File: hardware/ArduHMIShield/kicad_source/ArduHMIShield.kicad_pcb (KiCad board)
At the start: 2 copper layers, 72 x 53 mm, 49 parts, among them CN1 ARDUINO, Q1 2N7002, SW1 TAST_VER, SW2 TAST_VER, SW3 TAST_VER, SW4 TAST_VER, SW5 TAST_VER, SW6 TAST_VER, U1 LT1117, U2 74VHC245D

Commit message: updated design files to better support Aisler
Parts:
- C1, C10, C11, C2, C3, C4, C5, C6, C7, C8, C9: value 1u -> 1uF
- C12: value 100n -> 100nF
- R16: value DNI -> 0R
- R19: value 0R -> DNI
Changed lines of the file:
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@@
       (effects (font (size 1 1) (thickness 0.15)))
     )
-    (fp_text value 1u (at 0 1.9 270) (layer F.Fab)
+    (fp_text value 1uF (at 0 1.9 270) (layer F.Fab)
       (effects (font (size 1 1) (thickness 0.15)))
     )
@@
       (effects (font (size 1 1) (thickness 0.15)))
     )
-    (fp_text value 1u (at 0 1.9 270) (layer F.Fab)
+    (fp_text value 1uF (at 0 1.9 270) (layer F.Fab)
       (effects (font (size 1 1) (thickness 0.15)))
     )
@@
       (effects (font (size 1 1) (thickness 0.15)))
     )
-    (fp_text value 1u (at 0 1.9 270) (layer F.Fab)
+    (fp_text value 1uF (at 0 1.9 270) (layer F.Fab)
       (effects (font (size 1 1) (thickness 0.15)))
     )
@@
       (effects (font (size 1 1) (thickness 0.15)))
     )
-    (fp_text value 1u (at 0 1.9 270) (layer F.Fab)
+    (fp_text value 1uF (at 0 1.9 270) (layer F.Fab)
       (effects (font (size 1 1) (thickness 0.15)))
     )
@@
       (effects (font (size 1 1) (thickness 0.15)))
     )
-    (fp_text value 1u (at 0 1.9 180) (layer F.Fab)
+    (fp_text value 1uF (at 0 1.9 180) (layer F.Fab)
       (effects (font (size 1 1) (thickness 0.15)))
     )
@@
       (effects (font (size 1 1) (thickness 0.15)))
     )
-    (fp_text value 1u (at 0 1.9 270) (layer F.Fab)
+    (fp_text value 1uF (at 0 1.9 270) (layer F.Fab)
       (effects (font (size 1 1) (thickness 0.15)))
     )
@@
       (effects (font (size 1 1) (thickness 0.15)))
     )
-    (fp_text value 1u (at 0 1.9) (layer F.Fab)
+    (fp_text value 1uF (at 0 1.9) (layer F.Fab)
       (effects (font (size 1 1) (thickness 0.15)))
     )
@@
       (effects (font (size 1 1) (thickness 0.15)))
     )
-    (fp_text value 1u (at 0 1.9) (layer F.Fab)
+    (fp_text value 1uF (at 0 1.9) (layer F.Fab)
       (effects (font (size 1 1) (thickness 0.15)))
     )
@@
       (effects (font (size 1 1) (thickness 0.15)))
     )
-    (fp_text value 1u (at 0 1.9) (layer F.Fab)
+    (fp_text value 1uF (at 0 1.9) (layer F.Fab)
       (effects (font (size 1 1) (thickness 0.15)))
     )
@@
       (effects (font (size 1 1) (thickness 0.15)))
     )
-    (fp_text value 1u (at 0 1.9 180) (layer F.Fab)
+    (fp_text value 1uF (at 0 1.9 180) (layer F.Fab)
       (effects (font (size 1 1) (thickness 0.15)))
     )
@@
       (effects (font (size 1 1) (thickness 0.15)))
     )
-    (fp_text value 1u (at 0 1.9 180) (layer F.Fab)
+    (fp_text value 1uF (at 0 1.9 180) (layer F.Fab)
       (effects (font (size 1 1) (thickness 0.15)))
     )
@@
       (effects (font (size 1 1) (thickness 0.15)))
     )
-    (fp_text value 100n (at 0 1.9 90) (layer F.Fab)
+    (fp_text value 100nF (at 0 1.9 90) (layer F.Fab)
       (effects (font (size 1 1) (thickness 0.15)))
     )
@@
       (effects (font (size 1 1) (thickness 0.15)))
     )
-    (fp_text value DNI (at 0 1.9 180) (layer F.Fab)
+    (fp_text value 0R (at 0 1.9 180) (layer F.Fab)
       (effects (font (size 1 1) (thickness 0.15)))
     )
@@
       (effects (font (size 1 1) (thickness 0.15)))
     )
-    (fp_text value 0R (at 0 1.9 180) (layer F.Fab)
-      (effects (font (size 1 1) (thickness 0.15)))
-    )
+    (fp_text value DNI (at 0 1.9 180) (layer F.Fab)
+      (effects (font (size 1 1) (thickness 0.15)))
+    )

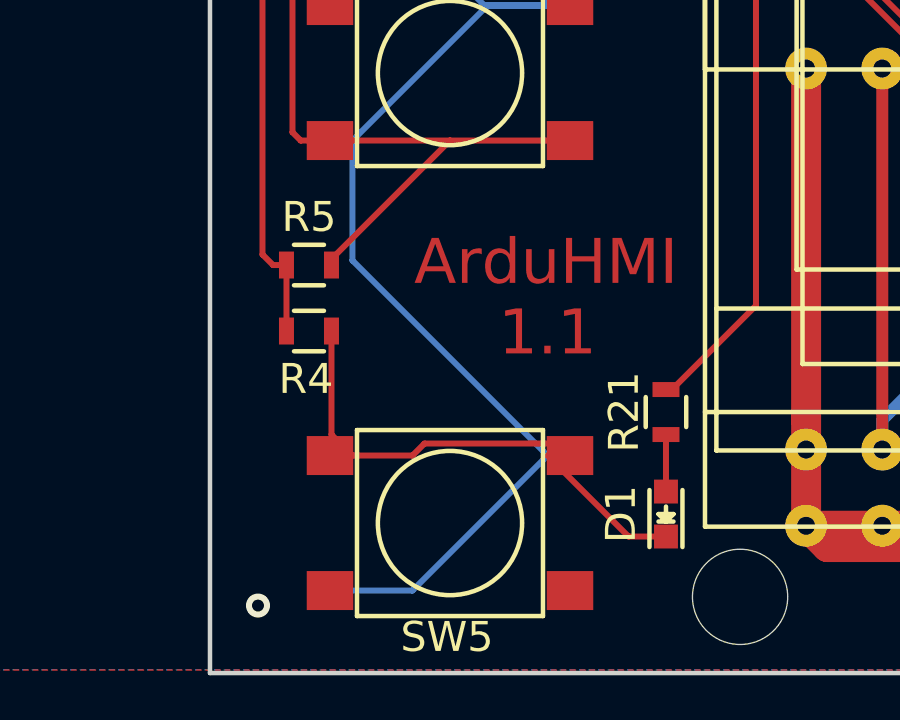
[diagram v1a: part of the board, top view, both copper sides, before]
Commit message: removed short cut, corrected silkscreen
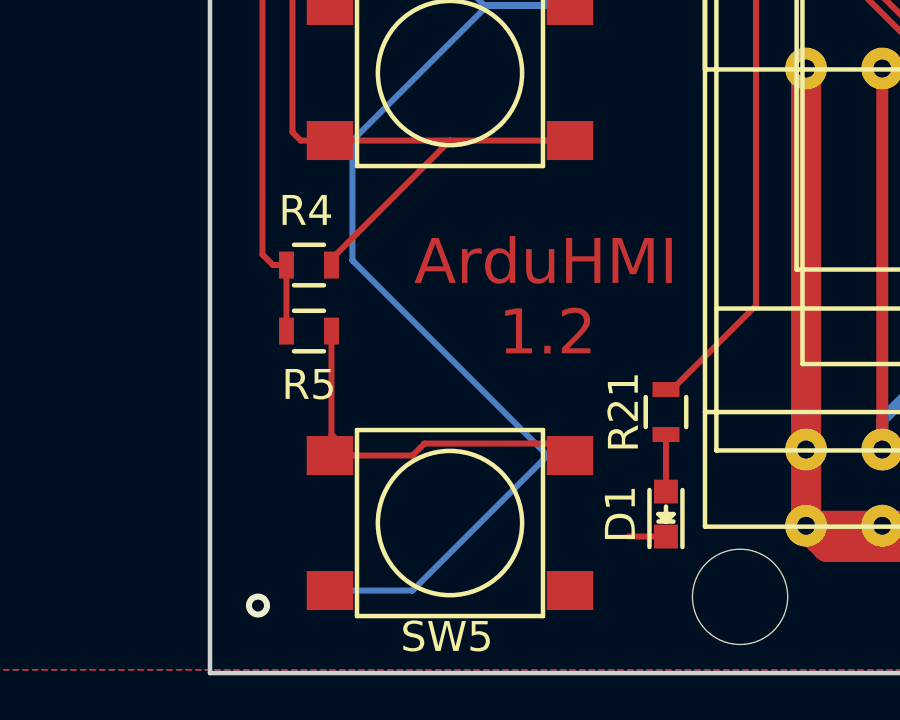
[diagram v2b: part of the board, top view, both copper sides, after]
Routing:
- net GND: track 248.6 -> 244.7 mm
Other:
- board text added: "1.2"
- board text removed: "1.1"
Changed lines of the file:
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@@
     (thickness 1.6)
     (drawings 17)
-    (tracks 516)
+    (tracks 515)
     (zones 0)
     (modules 49)
@@
     (tags "resistor 0603")
     (attr smd)
-    (fp_text reference R4 (at 0.1 -3.8 180) (layer F.SilkS)
+    (fp_text reference R4 (at 0.1 1.8 180) (layer F.SilkS)
       (effects (font (size 1 1) (thickness 0.15)))
     )
@@
     (tags "resistor 0603")
     (attr smd)
-    (fp_text reference R5 (at 0 -3.8) (layer F.SilkS)
+    (fp_text reference R5 (at 0 1.8) (layer F.SilkS)
       (effects (font (size 1 1) (thickness 0.15)))
     )
@@
     (effects (font (size 1.5 1.5) (thickness 0.3)) (justify left))
   )
-  (gr_text 1.1 (at 62.25 118.65) (layer F.Cu)
+  (gr_text 1.2 (at 62.25 118.65) (layer F.Cu)
     (effects (font (size 1.5 1.5) (thickness 0.3)))
   )
@@
   (segment (start 99.1 94.6) (end 104.1 89.6) (width 1) (layer B.Cu) (net 1))
   (segment (start 99.1 100.3) (end 99.1 94.6) (width 1) (layer B.Cu) (net 1))
-  (segment (start 64.95094 125.4493) (end 62.2512 122.74956) (width 0.2) (layer F.Cu) (net 1))
   (segment (start 66.2 125.4493) (end 64.95094 125.4493) (width 0.2) (layer F.Cu) (net 1))
   (via (at 52.5 80) (size 0.8) (drill 0.4) (layers F.Cu B.Cu) (net 1))

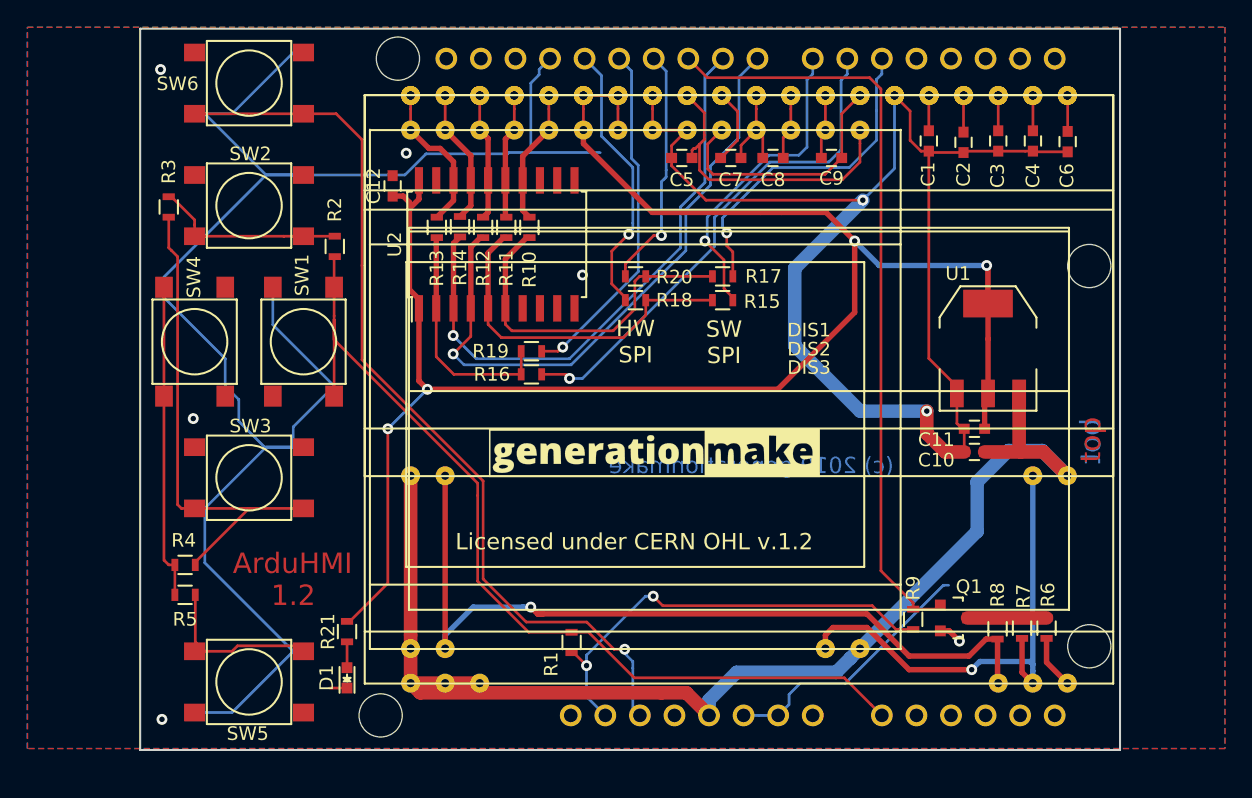
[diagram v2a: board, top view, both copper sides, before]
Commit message: added Arduino SPI header, updated all files
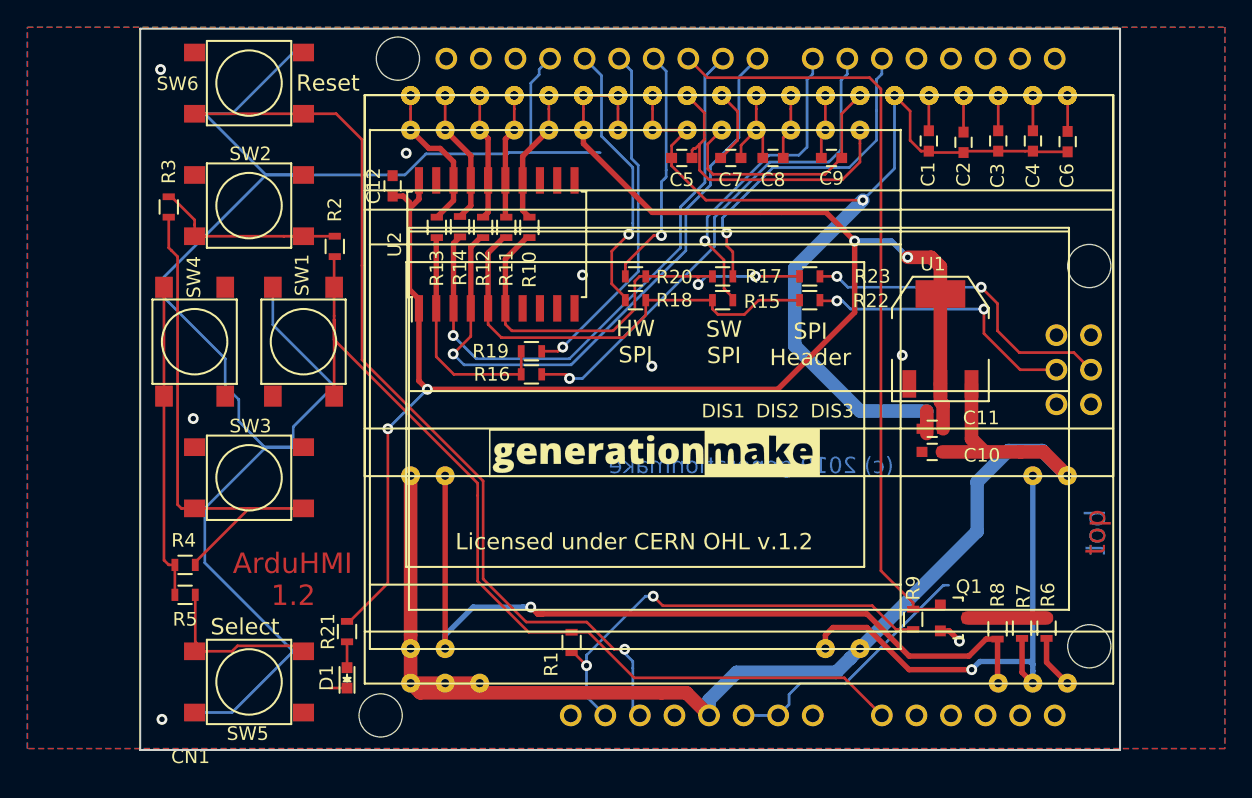
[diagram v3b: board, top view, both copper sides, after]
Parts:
- added R22: DNI, resistors:R_0603, F.Cu at (100.2, 97.0)
- added R23: DNI, resistors:R_0603, F.Cu at (100.2, 95.2)
- CN1: value ARDUINO -> ARDUINO_ISP; footprint MODULE_compute:ARDUINO -> MODULE_compute:ARDUINO_ISP
- moved U1 3.57 mm to (109.8, 99.8)
- moved C10 3.10 mm to (109.2, 108.1)
- moved C11 3.10 mm to (109.2, 106.4)
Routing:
- net GND: track 244.7 -> 218.2 mm, vias 8 -> 9
- net /ARDU_SI_3: track 0.00 -> 23.9 mm, vias 0 -> 2
- net /ARDU_CLK_3: track 0.00 -> 20.5 mm, vias 0 -> 2
- net +3V3: track 140.2 -> 127.3 mm
- net /ARDU_SI: track 25.5 -> 33.8 mm, vias 0 -> 2
- net /ARDU_CLK: track 25.7 -> 33.4 mm
- net +5V: track 111.4 -> 115.6 mm
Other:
- board text added: "Reset"
- board text added: "SPI Header"
- board text added: "Select"

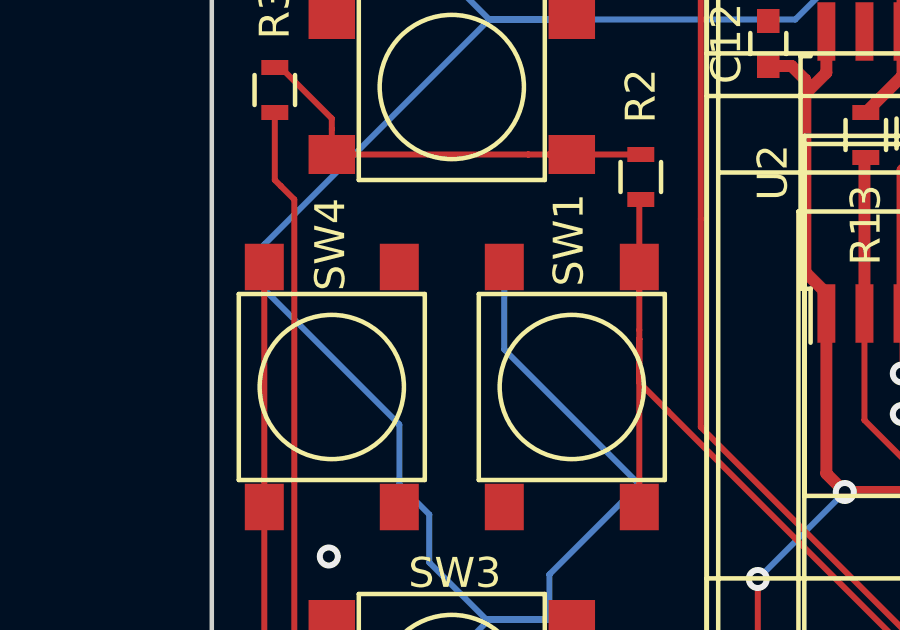
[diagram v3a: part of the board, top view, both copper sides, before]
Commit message: updated layout to get nicer 3D model
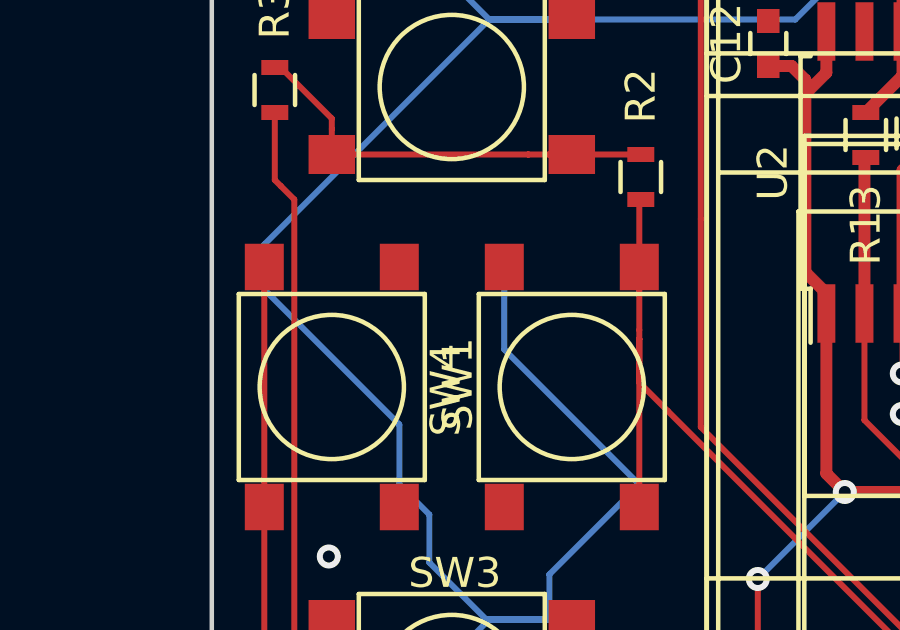
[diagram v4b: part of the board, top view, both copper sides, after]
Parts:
- CN1: footprint MODULE_compute:ARDUINO_ISP -> MODULE_compute:ARDUINO_ISP_TOP
- SW1, SW2, SW3, SW4, SW5: footprint mechanical-switches:WE_430182050816 -> mechanical-switches:WE_430182080816
